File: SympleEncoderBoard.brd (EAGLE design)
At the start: 50.8 x 50.8 mm, 31 parts, among them IC1 STM32F446RET6

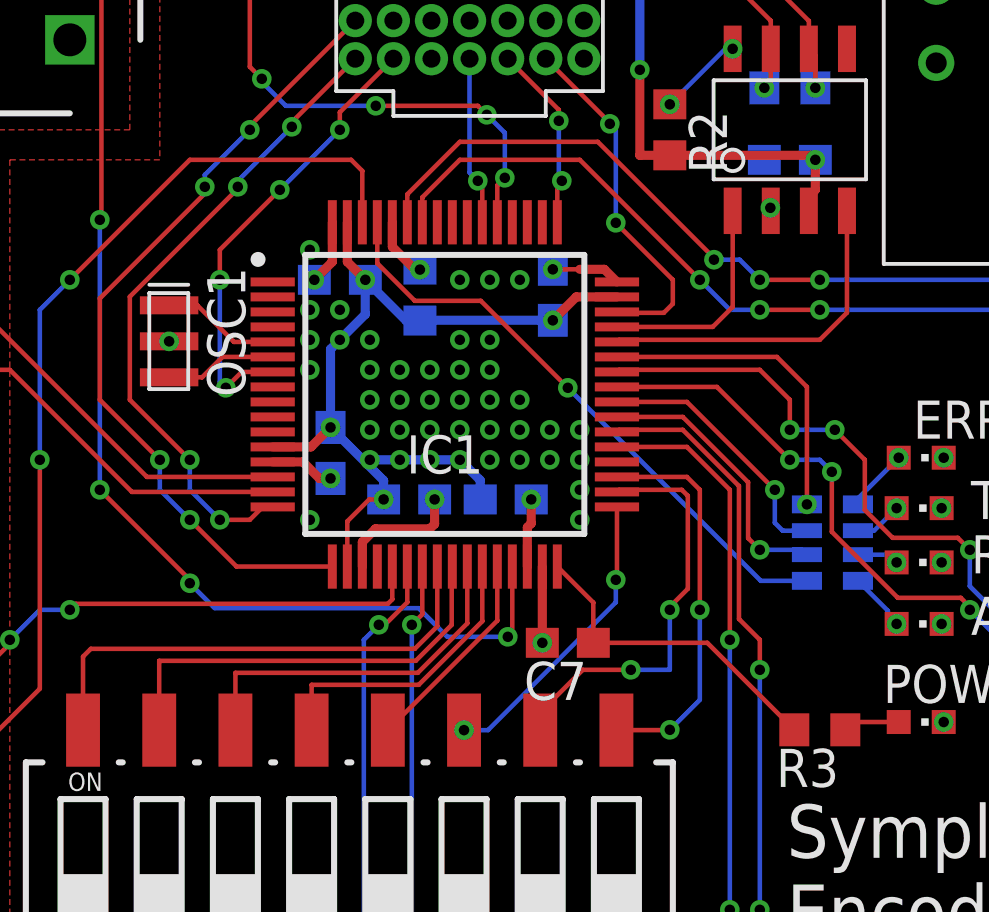
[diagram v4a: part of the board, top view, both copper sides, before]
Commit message: サーマルビアによる導通のエラーを直した
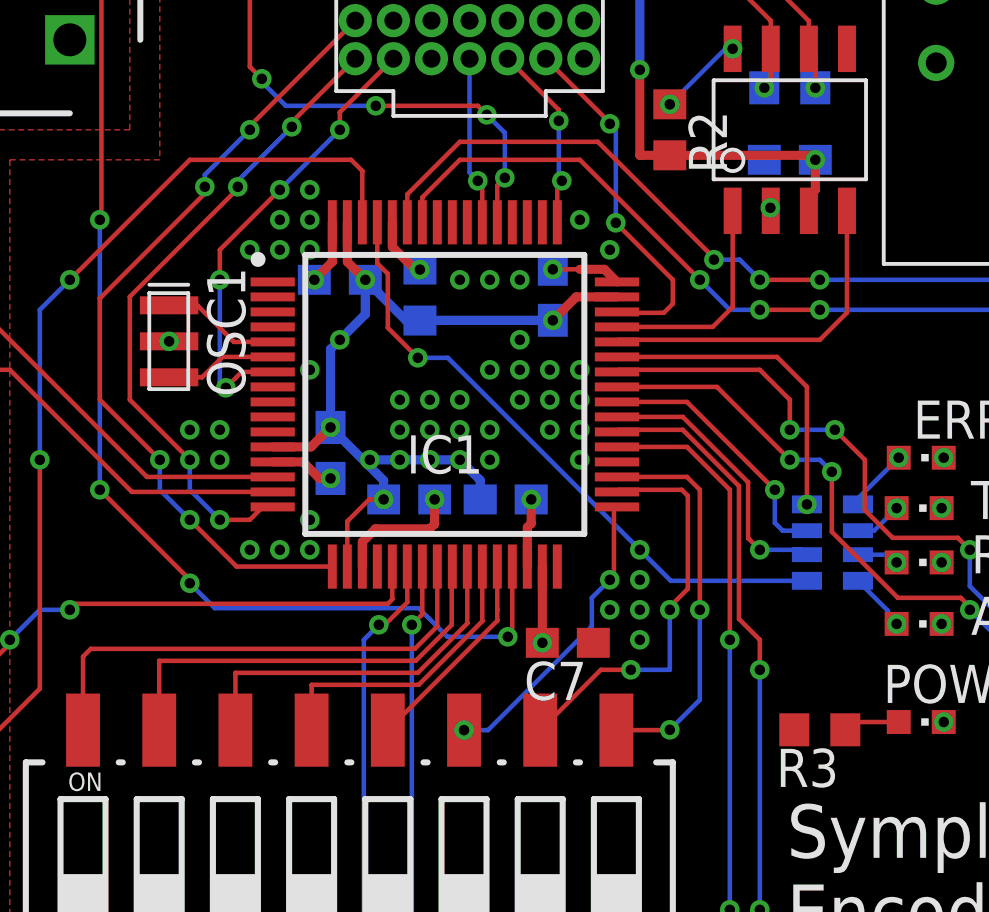
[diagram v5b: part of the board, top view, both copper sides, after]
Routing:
- net +3.3V: track 21.9 -> 10.9 mm
- net LEDGYRO: track 20.1 -> 21.1 mm, vias 1 -> 2
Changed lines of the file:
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@@
 <contactref element="IC1" pad="32"/>
 <contactref element="C7" pad="1"/>
-<wire x1="18.75" y1="32.918" x2="18.75" y2="31.6" width="0.3048" layer="1"/>
+<wire x1="18.75" y1="31.6" x2="18.75" y2="32.918" width="0.3048" layer="1"/>
 <wire x1="18.75" y1="31.6" x2="18.15" y2="31" width="0.3048" layer="1"/>
 <via x="18.15" y="31" extent="1-16" drill="0.35"/>
@@
 <wire x1="19.75" y1="22.26055" x2="19.75" y2="21.442" width="0.3048" layer="1"/>
 <wire x1="22" y1="22.7" x2="20.18945" y2="22.7" width="0.3048" layer="1"/>
-<wire x1="27.45" y1="20.242" x2="27.45" y2="18.9" width="0.1524" layer="1"/>
-<wire x1="27.45" y1="20.242" x2="26.25" y2="21.442" width="0.1524" layer="1"/>
-<wire x1="27.45" y1="18.9" x2="31.25" y2="18.9" width="0.1524" layer="1"/>
-<wire x1="31.25" y1="18.9" x2="34.15" y2="16" width="0.1524" layer="1"/>
 <polygon width="0.1524" layer="1" thermals="no" rank="3">
 <vertex x="8" y="7"/>
@@
 <contactref element="IC1" pad="61"/>
 <contactref element="R_I1" pad="5"/>
-<wire x1="34.57" y1="20.965" x2="33.035" y2="20.965" width="0.1524" layer="16"/>
-<wire x1="33.035" y1="20.965" x2="26.6" y2="27.4" width="0.1524" layer="16"/>
-<via x="26.6" y="27.4" extent="1-16" drill="0.35"/>
-<wire x1="26.6" y1="27.4" x2="23.7" y2="30.3" width="0.1524" layer="1"/>
-<wire x1="23.7" y1="30.3" x2="21.5" y2="30.3" width="0.1524" layer="1"/>
+<wire x1="34.57" y1="20.965" x2="30.035" y2="20.965" width="0.1524" layer="16"/>
+<wire x1="30.035" y1="20.965" x2="29" y2="22" width="0.1524" layer="16"/>
+<wire x1="29" y1="22" x2="27" y2="24" width="0.1524" layer="16"/>
+<wire x1="27" y1="24" x2="22.6" y2="28.4" width="0.1524" layer="16"/>
+<wire x1="22.6" y1="28.4" x2="21.6" y2="28.4" width="0.1524" layer="16"/>
+<via x="21.6" y="28.4" extent="1-16" drill="0.35"/>
+<wire x1="21.6" y1="28.4" x2="20.6" y2="29.4" width="0.1524" layer="1"/>
+<wire x1="20.6" y1="31.2" x2="20.6" y2="29.4" width="0.1524" layer="1"/>
+<wire x1="20.6" y1="31.2" x2="20.25" y2="31.55" width="0.1524" layer="1"/>
 <wire x1="20.25" y1="31.55" x2="20.25" y2="32.918" width="0.1524" layer="1"/>
-<wire x1="21.5" y1="30.3" x2="20.25" y2="31.55" width="0.1524" layer="1"/>
+<via x="29" y="22" extent="1-16" drill="0.35"/>
 </signal>
 <signal name="N$1">
@@
 <wire x1="28.7" y1="18" x2="30" y2="18" width="0.1524" layer="16"/>
 <via x="28.7" y="18" extent="1-16" drill="0.35"/>
-<wire x1="28.7" y1="18" x2="27.1" y2="18" width="0.1524" layer="1"/>
-<wire x1="27.1" y1="18" x2="25.68" y2="16.58" width="0.1524" layer="1"/>
-<wire x1="25.68" y1="16.58" x2="25.68" y2="15.99" width="0.1524" layer="1"/>
+<wire x1="28.7" y1="18" x2="27.7" y2="18" width="0.1524" layer="1"/>
+<wire x1="25.68" y1="15.99" x2="25.69" y2="15.99" width="0.1524" layer="1"/>
+<wire x1="27.7" y1="18" x2="25.69" y2="15.99" width="0.1524" layer="1"/>
 <wire x1="28.308" y1="24" x2="30.4" y2="24" width="0.1524" layer="1"/>
 <wire x1="30.6" y1="20.7" x2="30" y2="20.1" width="0.1524" layer="1"/>
@@
 <via x="23.14" y="15.99" extent="1-16" drill="0.35"/>
 <wire x1="23.14" y1="15.99" x2="23.94" y2="15.99" width="0.1524" layer="16"/>
-<wire x1="28.2" y1="20.25" x2="23.94" y2="15.99" width="0.1524" layer="16"/>
-<wire x1="28.2" y1="20.25" x2="28.2" y2="21" width="0.1524" layer="16"/>
-<via x="28.2" y="21" extent="1-16" drill="0.35"/>
-<wire x1="28.2" y1="21" x2="28.238" y2="21.038" width="0.1524" layer="1"/>
-<wire x1="28.238" y1="21.038" x2="28.238" y2="23.43" width="0.1524" layer="1"/>
+<wire x1="27.4" y1="19.45" x2="23.94" y2="15.99" width="0.1524" layer="16"/>
+<wire x1="28" y1="21" x2="27.4" y2="20.4" width="0.1524" layer="16"/>
+<wire x1="27.4" y1="20.4" x2="27.4" y2="19.45" width="0.1524" layer="16"/>
+<via x="28" y="21" extent="1-16" drill="0.35"/>
+<wire x1="28" y1="21" x2="28.138" y2="21.138" width="0.1524" layer="1"/>
+<wire x1="28.138" y1="23.33" x2="28.138" y2="21.138" width="0.1524" layer="1"/>
+<wire x1="28.138" y1="23.33" x2="28.238" y2="23.43" width="0.1524" layer="1"/>
 </signal>
 <signal name="N$2">
@@
 <contactref element="IC1" pad="28"/>
 <contactref element="S1" pad="12"/>
-<wire x1="24.25" y1="19.64" x2="24.25" y2="21.442" width="0.1524" layer="1"/>
+<wire x1="24.25" y1="19.64" x2="24.25" y2="20" width="0.1524" layer="1"/>
+<wire x1="24.25" y1="20" x2="24.25" y2="21.442" width="0.1524" layer="1"/>
 <wire x1="20.6" y1="15.99" x2="24.25" y2="19.64" width="0.1524" layer="1"/>
 </signal>
@@
 <via x="18" y="32" extent="1-16" drill="0.35"/>
 </signal>
-<signal name="N$10">
-<via x="18" y="30" extent="1-16" drill="0.35"/>
-</signal>
-<signal name="N$11">
-<via x="19" y="30" extent="1-16" drill="0.35"/>
-</signal>
-<signal name="N$12">
-<via x="18" y="29" extent="1-16" drill="0.35"/>
-</signal>
-<signal name="N$13">
-<via x="20" y="29" extent="1-16" drill="0.35"/>
-</signal>
 <signal name="N$14">
 <via x="18" y="28" extent="1-16" drill="0.35"/>
 </signal>
-<signal name="N$15">
-<via x="20" y="28" extent="1-16" drill="0.35"/>
-</signal>
-<signal name="N$16">
-<via x="21" y="28" extent="1-16" drill="0.35"/>
-</signal>
-<signal name="N$17">
-<via x="22" y="28" extent="1-16" drill="0.35"/>
-</signal>
-<signal name="N$18">
-<via x="23" y="28" extent="1-16" drill="0.35"/>
-</signal>
-<signal name="N$19">
-<via x="24" y="28" extent="1-16" drill="0.35"/>
-</signal>
-<signal name="N$20">
-<via x="24" y="29" extent="1-16" drill="0.35"/>
-</signal>
-<signal name="N$21">
-<via x="23" y="29" extent="1-16" drill="0.35"/>
-</signal>
-<signal name="N$22">
-<via x="20" y="27" extent="1-16" drill="0.35"/>
-</signal>
 <signal name="N$23">
 <via x="21" y="27" extent="1-16" drill="0.35"/>
@@
 <via x="22" y="27" extent="1-16" drill="0.35"/>
 </signal>
-<signal name="N$25">
-<via x="23" y="27" extent="1-16" drill="0.35"/>
-</signal>
-<signal name="N$26">
-<via x="24" y="27" extent="1-16" drill="0.35"/>
-</signal>
-<signal name="N$27">
-<via x="25" y="27" extent="1-16" drill="0.35"/>
-</signal>
 <signal name="N$28">
 <via x="26" y="26" extent="1-16" drill="0.35"/>
@@
 <via x="27" y="26" extent="1-16" drill="0.35"/>
 </signal>
-<signal name="N$30">
-<via x="25" y="26" extent="1-16" drill="0.35"/>
-</signal>
-<signal name="N$31">
-<via x="24" y="26" extent="1-16" drill="0.35"/>
-</signal>
 <signal name="N$32">
 <via x="23" y="26" extent="1-16" drill="0.35"/>
@@
 <via x="21" y="26" extent="1-16" drill="0.35"/>
 </signal>
-<signal name="N$35">
-<via x="20" y="26" extent="1-16" drill="0.35"/>
-</signal>
 <signal name="N$36">
 <via x="24" y="25" extent="1-16" drill="0.35"/>
 </signal>
-<signal name="N$37">
-<via x="25" y="25" extent="1-16" drill="0.35"/>
-</signal>
-<signal name="N$38">
-<via x="26" y="25" extent="1-16" drill="0.35"/>
-</signal>
 <signal name="N$39">
 <via x="27" y="25" extent="1-16" drill="0.35"/>
 </signal>
-<signal name="N$40">
-<via x="27" y="24" extent="1-16" drill="0.35"/>
-</signal>
-<signal name="N$41">
-<via x="27" y="23" extent="1-16" drill="0.35"/>
-</signal>
-<signal name="N$42">
-<via x="18" y="23" extent="1-16" drill="0.35"/>
-</signal>
 <signal name="N$43">
 <via x="23" y="31" extent="1-16" drill="0.35"/>
@@
 <via x="25" y="31" extent="1-16" drill="0.35"/>
 </signal>
+<signal name="N$19">
+<via x="25" y="27" extent="1-16" drill="0.35"/>
+</signal>
+<signal name="N$20">
+<via x="24" y="28" extent="1-16" drill="0.35"/>
+</signal>
+<signal name="N$10">
+<via x="26" y="28" extent="1-16" drill="0.35"/>
+</signal>
+<signal name="N$11">
+<via x="25" y="28" extent="1-16" drill="0.35"/>
+</signal>
+<signal name="N$12">
+<via x="26" y="27" extent="1-16" drill="0.35"/>
+</signal>
+<signal name="N$13">
+<via x="27" y="27" extent="1-16" drill="0.35"/>
+</signal>
+<signal name="N$15">
+<via x="27" y="28" extent="1-16" drill="0.35"/>
+</signal>
+<signal name="N$16">
+<via x="25" y="29" extent="1-16" drill="0.35"/>
+</signal>
+<signal name="N$17">
+<via x="23" y="27" extent="1-16" drill="0.35"/>
+</signal>
+<signal name="N$18">
+<via x="24" y="26" extent="1-16" drill="0.35"/>
+</signal>
+<signal name="N$22">
+<via x="18" y="23" extent="1-16" drill="0.35"/>
+</signal>
+<signal name="N$25">
+<via x="18" y="22" extent="1-16" drill="0.35"/>
+</signal>
+<signal name="N$26">
+<via x="17" y="22" extent="1-16" drill="0.35"/>
+</signal>
+<signal name="N$27">
+<via x="16" y="22" extent="1-16" drill="0.35"/>
+</signal>
+<signal name="N$30">
+<via x="16" y="32" extent="1-16" drill="0.35"/>
+</signal>
+<signal name="N$31">
+<via x="17" y="32" extent="1-16" drill="0.35"/>
+</signal>
+<signal name="N$35">
+<via x="18" y="33" extent="1-16" drill="0.35"/>
+</signal>
+<signal name="N$37">
+<via x="17" y="33" extent="1-16" drill="0.35"/>
+</signal>
+<signal name="N$38">
+<via x="18" y="34" extent="1-16" drill="0.35"/>
+</signal>
+<signal name="N$40">
+<via x="27" y="33" extent="1-16" drill="0.35"/>
+</signal>
+<signal name="N$41">
+<via x="28" y="32" extent="1-16" drill="0.35"/>
+</signal>
+<signal name="N$46">
+<via x="29" y="21" extent="1-16" drill="0.35"/>
+</signal>
+<signal name="N$47">
+<via x="29" y="20" extent="1-16" drill="0.35"/>
+</signal>
+<signal name="N$48">
+<via x="28" y="20" extent="1-16" drill="0.35"/>
+</signal>
+<signal name="N$49">
+<via x="29" y="19" extent="1-16" drill="0.35"/>
+</signal>
+<signal name="N$51">
+<via x="15" y="26" extent="1-16" drill="0.35"/>
+</signal>
+<signal name="N$52">
+<via x="14" y="26" extent="1-16" drill="0.35"/>
+</signal>
+<signal name="N$53">
+<via x="15" y="25" extent="1-16" drill="0.35"/>
+</signal>
 </signals>
